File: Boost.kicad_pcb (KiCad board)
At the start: 2 copper layers, 23 parts, among them Q1 IRFZ44N, U1 UC3843_DIP8

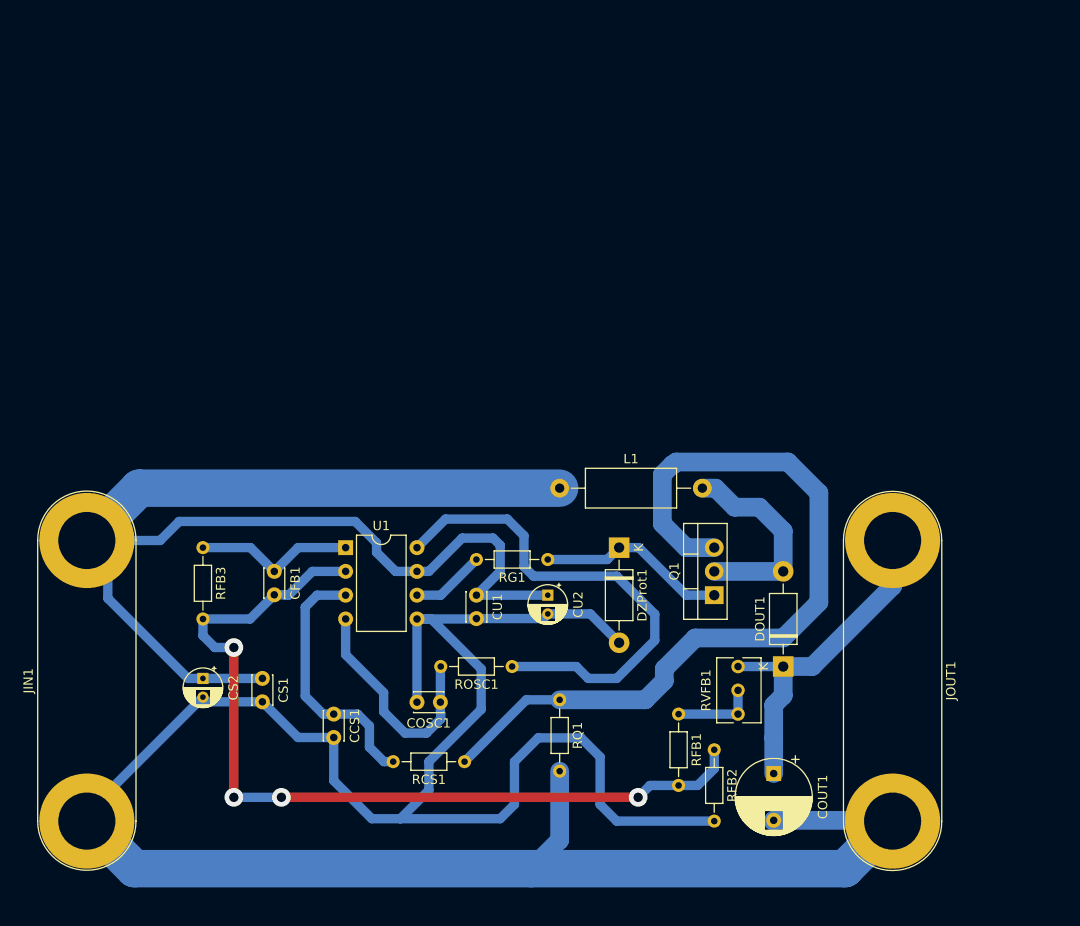
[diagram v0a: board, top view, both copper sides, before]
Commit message: Modificado PCB y esquemático según clase del 31/06/19
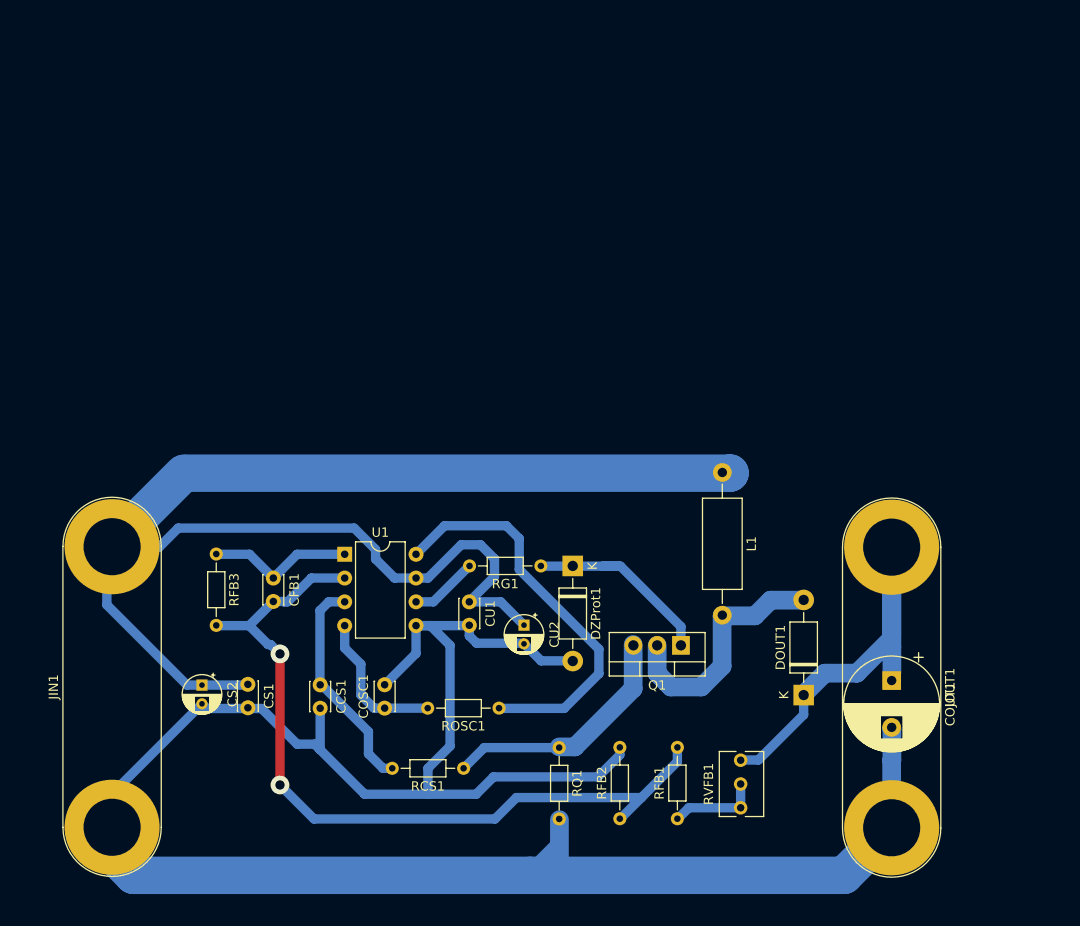
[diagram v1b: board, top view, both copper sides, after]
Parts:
- COUT1: value 100u -> 1000u; footprint Capacitor_THT:CP_Radial_D8.0mm_P5.00mm -> Capacitor_THT:CP_Radial_D10.0mm_P5.00mm
- DOUT1: value 1N5819 -> 1N5822
- RFB1: value 27k -> 22k
- RFB2: value 4k7 -> 3k3
- moved L1 17.5 mm to (175.9, 80.1), turned to 270 degrees
- moved COUT1 16.0 mm to (194.0, 102.3)
- moved RFB2 12.5 mm to (164.9, 117.1), turned to 90 degrees
- moved RFB1 11.2 mm to (171.1, 117.1), turned to 90 degrees
- moved RVFB1 10.0 mm to (177.8, 110.8)
- moved Q1 6.43 mm to (171.4, 98.6), turned to 180 degrees
- moved COSC1 5.99 mm to (139.8, 105.3), turned to 90 degrees
- moved DZProt1 5.33 mm to (159.9, 90.1)
- moved RQ1 5.11 mm to (158.4, 109.5)
- moved ROSC1 4.66 mm to (152.0, 105.3)
- moved CU2 4.09 mm to (154.7, 96.4)
- moved DOUT1 3.75 mm to (184.6, 103.9)
- moved CCS1 3.44 mm to (132.9, 102.8)
- moved JIN1 2.78 mm to (110.7, 118.0)
- moved CS1 1.67 mm to (125.2, 102.7)
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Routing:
- net Net-(Q1-Pad3): track 87.8 -> 26.4 mm
- net Earth: track 269.4 -> 231.6 mm
- net +15V: track 143.6 -> 156.7 mm
- net Net-(ROSC1-Pad1): track 53.0 -> 43.0 mm
- net Net-(COUT1-Pad1): track 36.8 -> 46.0 mm
- net Net-(COSC1-Pad1): track 24.9 -> 15.9 mm
- net Net-(CFB1-Pad2): track 93.6 -> 85.6 mm, vias 4 -> 2
- net Net-(CCS1-Pad1): track 28.0 -> 23.4 mm
- net Net-(DOUT1-Pad2): track 22.2 -> 26.3 mm
- net Net-(CFB1-Pad1): track 17.3 -> 15.9 mm
- net Net-(RFB1-Pad1): track 8.89 -> 9.67 mm
- net Net-(RG1-Pad2): track 7.93 -> 7.24 mm

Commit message: reemplazado IRFZ44N por IRFZ24N
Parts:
- Q1: value IRFZ44N -> IRFZ24N
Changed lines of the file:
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@@
   )
   (setup
-    (last_trace_width 1)
+    (last_trace_width 0.25)
     (user_trace_width 1)
     (user_trace_width 2)
@@
       (effects (font (size 1 1) (thickness 0.15)))
     )
-    (fp_text value IRFZ44N (at 2.54 2.5 180) (layer F.Fab)
-      (effects (font (size 1 1) (thickness 0.15)))
-    )
+    (fp_text value IRFZ24N (at 2.54 2.5 180) (layer F.Fab)
+      (effects (font (size 1 1) (thickness 0.15)))
+    )

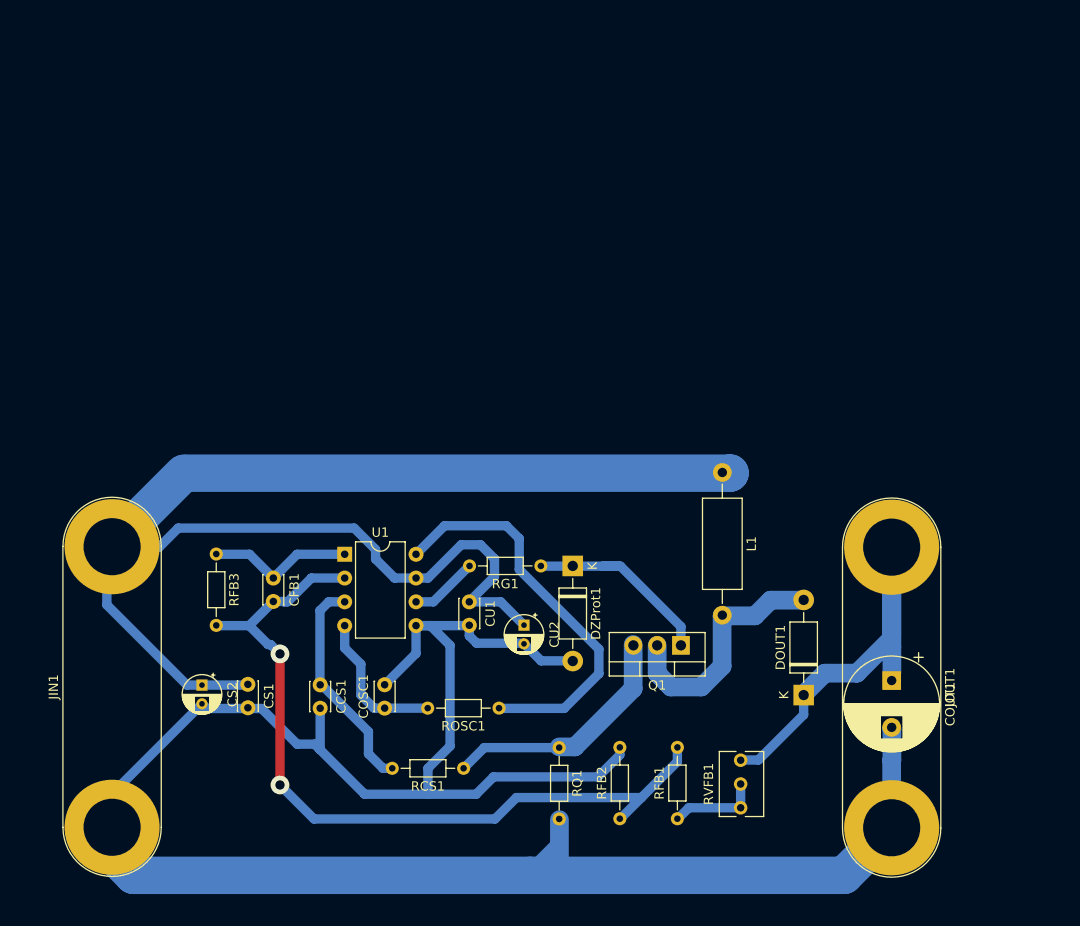
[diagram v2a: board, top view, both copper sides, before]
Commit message: modificado esquematico y pcb, pero falta modificar pcb
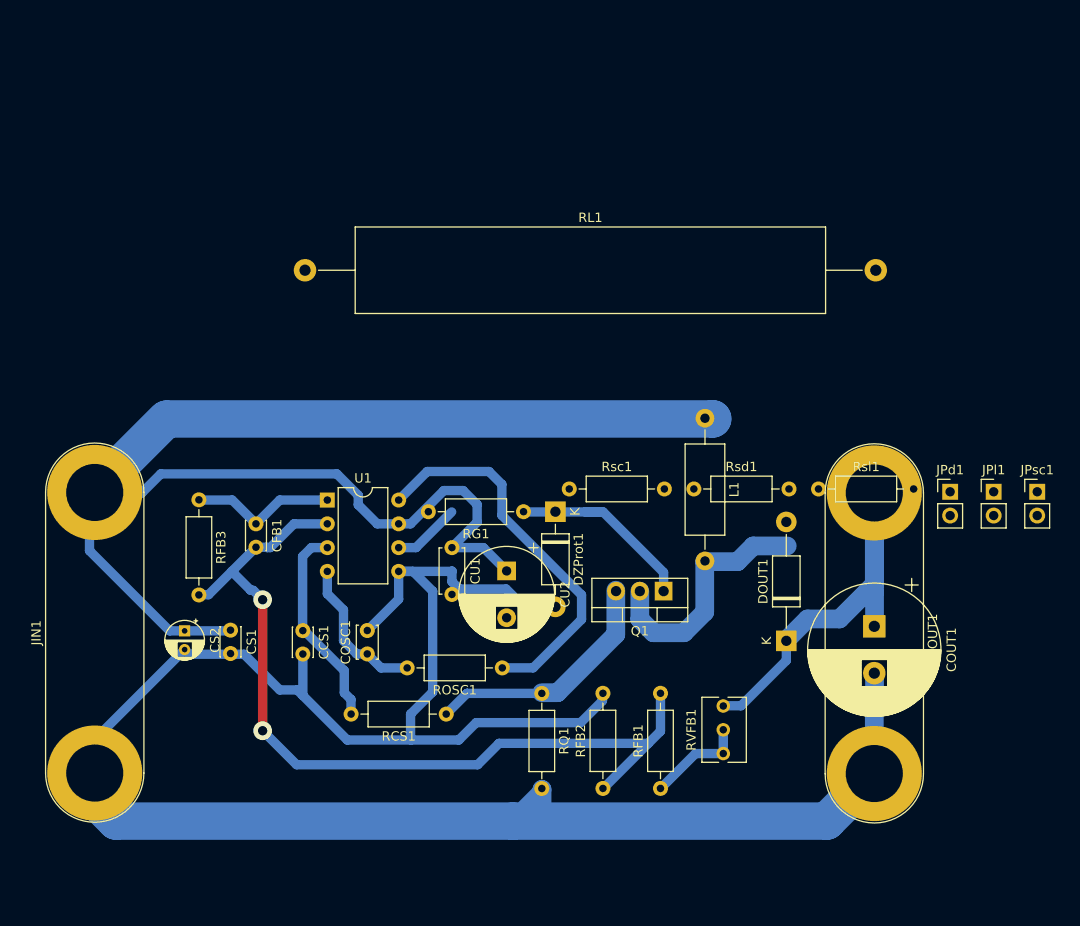
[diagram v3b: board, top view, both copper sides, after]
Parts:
- added JPd1: Jumper, Connector_PinHeader_2.54mm:PinHeader_1x02_P2.54mm_Vertical, F.Cu at (200.2, 82.2)
- added JPl1: Jumper, Connector_PinHeader_2.54mm:PinHeader_1x02_P2.54mm_Vertical, F.Cu at (204.9, 82.2)
- added JPsc1: Jumper, Connector_PinHeader_2.54mm:PinHeader_1x02_P2.54mm_Vertical, F.Cu at (209.5, 82.2)
- added RL1: 68, Resistor_THT:R_Axial_Power_L50.0mm_W9.0mm_P60.96mm, F.Cu at (131.3, 58.5)
- added Rsc1: 0,22, Resistor_THT:R_Axial_DIN0207_L6.3mm_D2.5mm_P10.16mm_Horizontal, F.Cu at (159.5, 81.9)
- added Rsd1: 0,22, Resistor_THT:R_Axial_DIN0207_L6.3mm_D2.5mm_P10.16mm_Horizontal, F.Cu at (172.8, 81.9)
- added Rsl1: 0,22, Resistor_THT:R_Axial_DIN0207_L6.3mm_D2.5mm_P10.16mm_Horizontal, F.Cu at (186.1, 81.9)
- COSC1: footprint Capacitor_THT:C_Disc_D3.0mm_W2.0mm_P2.50mm -> Capacitor_THT:C_Disc_D3.4mm_W2.1mm_P2.50mm
- COUT1: footprint Capacitor_THT:CP_Radial_D10.0mm_P5.00mm -> Capacitor_THT:CP_Radial_D14.0mm_P5.00mm
- CU1: footprint Capacitor_THT:C_Disc_D3.0mm_W2.0mm_P2.50mm -> Capacitor_THT:C_Disc_D4.7mm_W2.5mm_P5.00mm
- CU2: footprint Capacitor_THT:CP_Radial_D4.0mm_P2.00mm -> Capacitor_THT:CP_Radial_D10.0mm_P5.00mm
- DOUT1: footprint Diode_THT:D_DO-41_SOD81_P10.16mm_Horizontal -> Diode_THT:D_DO-41_SOD81_P12.70mm_Horizontal
- RCS1, RFB1, RFB2, RFB3, RG1, ROSC1, RQ1: footprint Resistor_THT:R_Axial_DIN0204_L3.6mm_D1.6mm_P7.62mm_Horizontal -> Resistor_THT:R_Axial_DIN0207_L6.3mm_D2.5mm_P10.16mm_Horizontal
- moved CCS1 6.08 mm to (131.1, 97.0)
- moved COSC1 6.08 mm to (137.9, 99.5)
- moved CU2 6.08 mm to (152.8, 90.6)
- moved CFB1 6.08 mm to (126.1, 85.6)
- moved COUT1 6.08 mm to (192.1, 96.5)
- moved DZProt1 6.08 mm to (158.0, 84.3)
- moved JOUT1 6.08 mm to (192.1, 82.3)
- moved Q1 6.08 mm to (169.6, 92.8)
- moved RFB3 6.08 mm to (120.0, 83.0)
- moved RG1 6.08 mm to (154.6, 84.3)
- moved RVFB1 6.08 mm to (176.0, 105.1)
- moved CS1 6.08 mm to (123.3, 97.0)
- moved JIN1 6.08 mm to (108.8, 112.2)
- moved CS2 6.08 mm to (118.4, 97.0)
- moved CU1 6.08 mm to (147.0, 88.1)
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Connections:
- DOUT1 pad 1: Net-(COUT1-Pad1) -> Net-(DOUT1-Pad1)
- JOUT1 pad 1: Net-(COUT1-Pad1) -> Net-(DOUT1-Pad1)
- L1 pad 2: Net-(DOUT1-Pad2) -> Net-(JPl1-Pad2)
- Q1 pad 2: Net-(DOUT1-Pad2) -> Net-(JPd1-Pad1)
- RVFB1 pad 1: Net-(COUT1-Pad1) -> Net-(DOUT1-Pad1)
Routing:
- net Net-(CFB1-Pad2): track 85.6 -> 91.8 mm
- net Earth: track 231.6 -> 229.0 mm
- net Net-(CCS1-Pad1): track 23.4 -> 21.8 mm
- net Net-(ROSC1-Pad1): track 43.0 -> 41.4 mm
- net Net-(RFB1-Pad1): track 9.67 -> 10.8 mm

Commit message: acomodado pcb a 10x10 con bobina casi de la medida y disipador del FET, resta corroborar medidas de los mismos
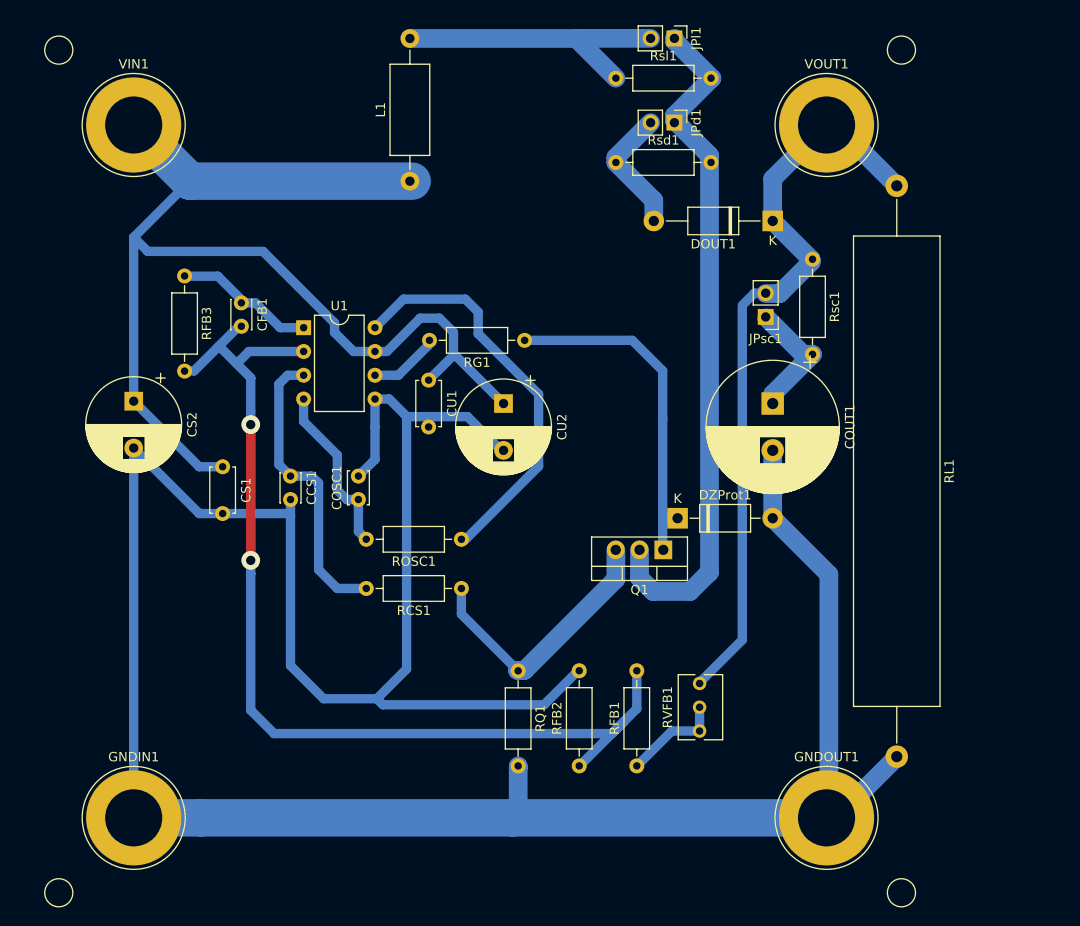
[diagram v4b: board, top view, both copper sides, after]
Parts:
- removed JIN1, JOUT1: Conn_01x02, Connector:Banana_Jack_2Pin
- added GNDIN1: Conn_01x01_MountingPin, Connector:Banana_Jack_1Pin, F.Cu at (113.0, 117.0)
- added GNDOUT1: Conn_01x01_MountingPin, Connector:Banana_Jack_1Pin, F.Cu at (187.0, 117.0)
- added VIN1: Conn_01x01_MountingPin, Connector:Banana_Jack_1Pin, F.Cu at (113.0, 43.0)
- added VOUT1: Conn_01x01_MountingPin, Connector:Banana_Jack_1Pin, F.Cu at (187.0, 43.0)
- CS1: footprint Capacitor_THT:C_Disc_D3.0mm_W2.0mm_P2.50mm -> Capacitor_THT:C_Disc_D4.7mm_W2.5mm_P5.00mm
- CS2: footprint Capacitor_THT:CP_Radial_D4.0mm_P2.00mm -> Capacitor_THT:CP_Radial_D10.0mm_P5.00mm
- moved RL1 63.8 mm to (194.5, 49.5), turned to 270 degrees
- moved JPl1 59.2 mm to (170.8, 33.8), turned to 270 degrees
- moved JPd1 49.2 mm to (170.8, 42.8), turned to 270 degrees
- moved Rsl1 48.9 mm to (164.5, 38.0)
- moved DOUT1 44.9 mm to (181.2, 53.2), turned to 180 degrees
- moved L1 40.4 mm to (142.5, 49.0), turned to 90 degrees
- moved Rsd1 35.9 mm to (164.5, 47.0)
- moved Rsc1 35.7 mm to (185.5, 57.3), turned to 270 degrees
- moved JPsc1 34.5 mm to (180.5, 63.5), turned to 180 degrees
- moved COUT1 26.2 mm to (181.2, 72.8)
- moved CS2 25.1 mm to (113.0, 72.5)
- moved RFB3 24.0 mm to (118.4, 59.1)
- moved CFB1 23.6 mm to (124.5, 62.0)
- moved U1 18.6 mm to (131.2, 64.6)
- moved RG1 18.3 mm to (154.8, 66.0)
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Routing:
- net Net-(DOUT1-Pad1): track 0.00 -> 79.1 mm
- net Net-(JPd1-Pad1): track 0.00 -> 74.2 mm
- net Earth: track 229.0 -> 299.6 mm
- net Net-(COUT1-Pad1): track 46.0 -> 13.5 mm
- net Net-(JPl1-Pad2): track 0.00 -> 31.7 mm
- net +15V: track 156.7 -> 125.7 mm
- net Net-(CFB1-Pad2): track 91.8 -> 110.4 mm
- net Net-(DZProt1-Pad1): track 20.7 -> 37.4 mm
- net Net-(DOUT1-Pad2): track 26.3 -> 13.7 mm
- net Net-(CCS1-Pad1): track 21.8 -> 31.8 mm
- net Net-(Q1-Pad3): track 26.4 -> 29.4 mm
- net Net-(COSC1-Pad1): track 16.1 -> 18.5 mm
- net Net-(ROSC1-Pad1): track 41.4 -> 43.5 mm
- net Net-(CFB1-Pad1): track 15.9 -> 14.9 mm
